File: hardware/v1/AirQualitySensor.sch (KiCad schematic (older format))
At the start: 1 part

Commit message: Start schematic
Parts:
- added DS1: EA_DOGM132W-5, AirQualitySensor:EA_DOGM132W-5, symbol AirQualitySensor:EA_DOGM132W-5
- added U1: 004-0-0053, AirQualitySensor:Senseair_S8_Up, symbol AirQualitySensor:004-0-0053
- added U2: DHT22, AirQualitySensor:DHT22, symbol AirQualitySensor:DHT22
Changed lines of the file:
@@
 NoConn ~ 5000 2150
 NoConn ~ 5000 2050
+$Comp
+L AirQualitySensor:EA_DOGM132W-5 DS1
+U 1 1 615E0422
+P 7350 2150
+F 0 "DS1" H 7950 2415 50  0000 C CNN
+F 1 "EA_DOGM132W-5" H 7950 2324 50  0000 C CNN
+F 2 "AirQualitySensor:EA_DOGM132W-5" H 8400 2250 50  0001 L CNN
+F 3 "" H 8400 2150 50  0001 L CNN
+F 4 "LCD Graphic Display Modules & Accessories DOGM Grapic 132x32 White Background" H 8400 2050 50  0001 L CNN "Description"
+F 5 "2" H 8400 1950 50  0001 L CNN "Height"
+F 6 "790-EADOGM132W5" H 8400 1850 50  0001 L CNN "Mouser Part Number"
+F 7 "https://www.mouser.co.uk/ProductDetail/ELECTRONIC-ASSEMBLY/EA-DOGM132W-5?qs=s9z6UkyjM7o689ToJkW0yA%3D%3D" H 8400 1750 50  0001 L CNN "Mouser Price/Stock"
+F 8 "ELECTRONIC ASSEMBLY" H 8400 1650 50  0001 L CNN "Manufacturer_Name"
+F 9 "EA DOGM132W-5" H 8400 1550 50  0001 L CNN "Manufacturer_Part_Number"
+	1    7350 2150
+	1    0    0    -1
+$EndComp
+$Comp
+L AirQualitySensor:004-0-0053 U1
+U 1 1 615E61D2
+P 3950 5000
+F 0 "U1" H 3950 5581 50  0000 C CNN
+F 1 "004-0-0053" H 3950 5490 50  0000 C CNN
+F 2 "AirQualitySensor:Senseair_S8_Up" H 3950 5000 50  0001 C CNN
+F 3 "https://rmtplusstoragesenseair.blob.core.windows.net/docs/publicerat/PSP126.pdf" H 3950 5000 50  0001 C CNN
+	1    3950 5000
+	1    0    0    -1
+$EndComp
+$Comp
+L AirQualitySensor:DHT22 U2
+U 1 1 615E6A6B
+P 5750 4550
+F 0 "U2" H 6278 4446 50  0000 L CNN
+F 1 "DHT22" H 6278 4355 50  0000 L CNN
+F 2 "AirQualitySensor:DHT22" H 6500 4050 50  0001 C CNN
+F 3 "https://www.sparkfun.com/datasheets/Sensors/Temperature/DHT22.pdf" H 6500 4050 50  0001 C CNN
+	1    5750 4550
+	1    0    0    -1
+$EndComp
 $EndSCHEMATC

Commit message: More Layout work
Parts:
- added C1, C2: 1u, Capacitor_SMD:C_0603_1608Metric, symbol Device:C_Small
- added C10, C11, C12, C13, C6, C7, C8, C9: 1u, Capacitor_SMD:C_0402_1005Metric, symbol Device:C_Small
- added C3, C4: 4u7, Capacitor_SMD:C_0603_1608Metric, symbol Device:C_Small
- added C5: 100u, Capacitor_SMD:C_0402_1005Metric, symbol Device:C_Small
- added FB1, FB2: 100R, Inductor_SMD:L_0603_1608Metric, symbol Device:Ferrite_Bead_Small
- added J1: USB_C_Receptacle_USB2.0, Connector_USB:USB_C_Receptacle_HRO_TYPE-C-31-M-12, symbol Connector:USB_C_Receptacle_USB2.0
- added R1, R2: 5.1k, Resistor_SMD:R_0402_1005Metric, symbol Device:R_Small
- added R3, R4, R5: 10k, Resistor_SMD:R_0402_1005Metric, symbol Device:R_Small
- added U3: XC6206P332MR, Package_TO_SOT_SMD:SOT-23, symbol Regulator_Linear:XC6206PxxxMR
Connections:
- net +3V3: now also DS1.34 (VDD2), DS1.35 (VDD), C2.1, C4.1, C5.1, R3.1, R4.1, R5.1, U3.2 (VO)
- net +5V: now also U1.1 (G+), U2.1 (VDD), C3.1, FB1.1; no longer A1.22 (VBUS)
- net GND: now also DS1.26 (VSS_1), DS1.33 (VSS_2), U1.2 (G0), U2.4 (GND), C1.1, C10.1, C11.1, C12.2, C13.1, C2.2, C3.2, C4.2, C5.2, C6.1, C8.1, J1.A1 (GND), J1.A12 (GND), J1.B1 (GND), J1.B12 (GND), R1.2, R2.1, U3.1 (GND)
- net USB_D-: now reaches A1.23 (D-)
- net USB_D-: now also J1.A7 (D-), J1.B7 (D-)
- net USB_D+: now reaches A1.24 (D+)
- net USB_D+: now also J1.A6 (D+), J1.B6 (D+)
- net at DS1.21 (V0): now also C13.2
- net at DS1.22 (V1): now also C11.2
- net at DS1.23 (V2): now also C10.2
- net at DS1.24 (V3): now also C8.2
- net at DS1.25 (V4): now also C6.2
- net at DS1.27 (CAP2N): now also C7.1
- net at DS1.28 (CAP2P): now also C7.2
- net at DS1.29 (CAP1P): now also C9.1
- net at DS1.30 (CAP1N): now also C9.2
- net at DS1.31 (CAP3P): now also DS1.32 (VOUT), C12.1
- net DISP_SI: now reaches DS1.36 (SI)
- net DISP_SCL: now reaches DS1.37 (SCL)
- net DISP_A0: now reaches DS1.38 (A0)
- net DISP_RST: now reaches DS1.39 (RST)
- net DISP_CS: now reaches DS1.40 (CS1B)
- net S8_RXD: now reaches U1.7 (UART_TXD)
- net S8_RXD: now also R3.2
- net S8_TXD: now reaches U1.8 (UART_RXD)
- net S8_TXD: now also R4.2
- net DHT22: now reaches U2.2 (DATA)
- net DHT22: now also R5.2
- new net: J1.A5 (CC1), R1.1
- new net: J1.B5 (CC2), R2.2
- new net: C1.2, FB2.1, U3.3 (VI)
- new net VBUS: A1.22 (VBUS), FB1.2, FB2.2, J1.A4 (VBUS), J1.A9 (VBUS), J1.B4 (VBUS), J1.B9 (VBUS)
- no-connect marks 28 -> 40
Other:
- moved on the sheet: A1, DS1, U1, U2

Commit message: Continue schematic
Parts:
- added C14: 100u, Capacitor_SMD:C_0402_1005Metric, symbol Device:C_Small
- added J2: SWD, AirQualitySensor:TC2030-IDC-FP, symbol AirQualitySensor:TC2030
- added J3: UART, Connector_PinHeader_2.54mm:PinHeader_1x06_P2.54mm_Vertical, symbol AirQualitySensor:UART_ftdi
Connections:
- net +3V3: now also C14.2, J2.1 (VCC)
- net GND: now also C14.1, J2.5 (GND), J3.1 (GND)
- net VBUS: now also J3.3 (VCC)
- net RESET: now reaches A1.21 (P0.18/Reset)
- net RESET: now also J2.3 (nRESET)
- net SWD_SWO: now reaches A1.27 (SWO/P1.00)
- net SWD_SWO: now also J2.6 (SWO)
- net SWD_SWCLK: now reaches A1.31 (SWDCLK)
- net SWD_SWCLK: now also J2.4 (SWCLK)
- net SWD_SWDIO: now reaches A1.32 (SWDIO)
- net SWD_SWDIO: now also J2.2 (SWDIO)
- new net UART_RXD: J3.4 (TXD)
- new net UART_TXD: J3.5 (RXD)
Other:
- note added: "Display"
- note added: "Power & USB"
- note added: "Programming Connectors"
- note added: "Sensors"
- moved on the sheet: A1, C1, C10, C11, C12, C13, C2, C3, C4, C5, C6, C7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

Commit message: More layouting
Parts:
- added D1: Red, LED_THT:LED_D3.0mm, symbol Device:LED_Small
- added D2: Yellow, LED_THT:LED_D3.0mm, symbol Device:LED_Small
- added D3: Green, LED_THT:LED_D3.0mm, symbol Device:LED_Small
- added H1, H2, H3: MountingHole, MountingHole:MountingHole_2.5mm_Pad, symbol Mechanical:MountingHole_Pad
- added R6, R7: 10k, Resistor_SMD:R_0402_1005Metric, symbol Device:R_Small
- added R8: 100k, Resistor_SMD:R_0402_1005Metric, symbol Device:R_Small
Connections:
- net +3V3: now also C14.1, C5.2; no longer C14.2, C5.1
- net GND: now also C10.2, C11.2, C12.1, C13.2, C14.2, C5.1, C6.2, C8.2, R2.2, D1.1 (K), D2.1 (K), D3.1 (K); no longer C10.1, C11.1, C12.2, C13.1, C14.1, C5.2, C6.1, C8.1, R2.1
- net at DS1.21 (V0): now also C13.1; no longer C13.2
- net at DS1.22 (V1): now also C11.1; no longer C11.2
- net at DS1.23 (V2): now also C10.1; no longer C10.2
- net at DS1.24 (V3): now also C8.1; no longer C8.2
- net at DS1.25 (V4): now also C6.1; no longer C6.2
- net at DS1.27 (CAP2N): now also C7.2; no longer C7.1
- net at DS1.28 (CAP2P): now also C7.1; no longer C7.2
- net at DS1.29 (CAP1P): now also C9.2; no longer C9.1
- net at DS1.30 (CAP1N): now also C9.1; no longer C9.2
- net at DS1.31 (CAP3P), DS1.32 (VOUT): now also C12.2; no longer C12.1
- net at J1.B5 (CC2): now also R2.1; no longer R2.2
- new net: D1.2 (A), R6.1
- new net: D2.2 (A), R7.1
- new net: D3.2 (A), R8.1
- new net LED_GREEN: R8.2
- new net LED_RED: R6.2
- new net LED_YELLOW: R7.2
- no-connect marks 40 -> 43
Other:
- note added: "LEDs"
- moved on the sheet: C14
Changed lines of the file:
@@
 U 1 1 616037F6
 P 2100 1350
-F 0 "R2" H 2150 1450 50  0000 L CNN
-F 1 "5.1k" V 2200 1200 50  0000 L CNN
+F 0 "R2" H 2150 1250 50  0000 L CNN
+F 1 "5.1k" V 2200 1500 50  0000 R CNN
 F 2 "Resistor_SMD:R_0402_1005Metric" H 2100 1350 50  0001 C CNN
 F 3 "~" H 2100 1350 50  0001 C CNN
 	1    2100 1350
-	0    1    1    0
+	0    -1   1    0
 $EndComp
 $Comp
@@
 F 3 "~" H 8950 2800 50  0001 C CNN
 	1    8950 2800
-	-1   0    0    1
+	-1   0    0    -1
 $EndComp
 $Comp
@@
 F 3 "~" H 8700 2700 50  0001 C CNN
 	1    8700 2700
-	-1   0    0    1
+	-1   0    0    -1
 $EndComp
 $Comp
@@
 F 3 "~" H 9200 2900 50  0001 C CNN
 	1    9200 2900
-	-1   0    0    1
+	-1   0    0    -1
 $EndComp
 $Comp
@@
 F 3 "~" H 9450 3000 50  0001 C CNN
 	1    9450 3000
-	-1   0    0    1
+	-1   0    0    -1
 $EndComp
 $Comp
@@
 F 3 "~" H 9700 3100 50  0001 C CNN
 	1    9700 3100
-	-1   0    0    1
+	-1   0    0    -1
 $EndComp
 Wire Wire Line
@@
 F 3 "~" H 9500 1850 50  0001 C CNN
 	1    9500 1850
-	-1   0    0    1
+	-1   0    0    -1
 $EndComp
 Wire Wire Line
@@
 F 3 "~" H 9100 2050 50  0001 C CNN
 	1    9100 2050
-	0    -1   1    0
+	0    1    1    0
 $EndComp
 $Comp
@@
 F 3 "~" H 8850 2250 50  0001 C CNN
 	1    8850 2250
-	0    -1   -1   0
+	0    1    -1   0
 $EndComp
 Wire Wire Line
@@
 Wire Wire Line
 	9000 2150 9000 2050
-Wire Wire Line
-	9000 2150 9750 2150
 Wire Wire Line
 	9750 2250 8950 2250
@@
 F 3 "~" H 5350 5450 50  0001 C CNN
 	1    5350 5450
-	1    0    0    -1
+	1    0    0    1
 $EndComp
 $Comp
@@
 Wire Wire Line
 	5350 5200 5350 5350
-Connection ~ 5350 5350
 Wire Wire Line
 	5250 5350 5350 5350
-Wire Wire Line
-	8750 2350 9750 2350
-Wire Wire Line
-	9350 1750 9500 1750
-Connection ~ 9500 1750
-Wire Wire Line
-	9500 1750 9750 1750
 $Comp
 L AirQualitySensor:TC2030 J2
@@
 L Device:C_Small C14
 U 1 1 617462A1
-P 8950 1150
-F 0 "C14" H 9042 1196 50  0000 L CNN
-F 1 "100u" H 9042 1105 50  0000 L CNN
-F 2 "Capacitor_SMD:C_0402_1005Metric" H 8950 1150 50  0001 C CNN
-F 3 "~" H 8950 1150 50  0001 C CNN
-	1    8950 1150
-	-1   0    0    1
+P 8850 1150
+F 0 "C14" H 8942 1196 50  0000 L CNN
+F 1 "100u" H 8942 1105 50  0000 L CNN
+F 2 "Capacitor_SMD:C_0402_1005Metric" H 8850 1150 50  0001 C CNN
+F 3 "~" H 8850 1150 50  0001 C CNN
+	1    8850 1150
+	1    0    0    -1
 $EndComp
 $Comp
 L power:+3V3 #PWR0129
 U 1 1 617473D8
-P 8950 1050
-F 0 "#PWR0129" H 8950 900 50  0001 C CNN
-F 1 "+3V3" H 8800 1150 50  0000 C CNN
-F 2 "" H 8950 1050 50  0001 C CNN
-F 3 "" H 8950 1050 50  0001 C CNN
-	1    8950 1050
+P 8850 1050
+F 0 "#PWR0129" H 8850 900 50  0001 C CNN
+F 1 "+3V3" H 8700 1150 50  0000 C CNN
+F 2 "" H 8850 1050 50  0001 C CNN
+F 3 "" H 8850 1050 50  0001 C CNN
+	1    8850 1050
 	1    0    0    -1
 $EndComp
@@
 L power:GND #PWR0130
 U 1 1 6174788F
-P 8950 1250
-F 0 "#PWR0130" H 8950 1000 50  0001 C CNN
-F 1 "GND" H 9000 1100 50  0000 R CNN
-F 2 "" H 8950 1250 50  0001 C CNN
-F 3 "" H 8950 1250 50  0001 C CNN
-	1    8950 1250
-	1    0    0    -1
-$EndComp
+P 8850 1250
+F 0 "#PWR0130" H 8850 1000 50  0001 C CNN
+F 1 "GND" H 8900 1100 50  0000 R CNN
+F 2 "" H 8850 1250 50  0001 C CNN
+F 3 "" H 8850 1250 50  0001 C CNN
+	1    8850 1250
+	1    0    0    -1
+$EndComp
+$Comp
+L Device:LED_Small D1
+U 1 1 61768156
+P 1050 5600
+F 0 "D1" V 1096 5530 50  0000 R CNN
+F 1 "Red" V 1005 5530 50  0000 R CNN
+F 2 "LED_THT:LED_D3.0mm" V 1050 5600 50  0001 C CNN
+F 3 "~" V 1050 5600 50  0001 C CNN
+	1    1050 5600
+	0    -1   -1   0
+$EndComp
+$Comp
+L Device:LED_Small D2
+U 1 1 61768FD8
+P 1500 5600
+F 0 "D2" V 1546 5530 50  0000 R CNN
+F 1 "Yellow" V 1455 5530 50  0000 R CNN
+F 2 "LED_THT:LED_D3.0mm" V 1500 5600 50  0001 C CNN
+F 3 "~" V 1500 5600 50  0001 C CNN
+	1    1500 5600
+	0    -1   -1   0
+$EndComp
+$Comp
+L Device:LED_Small D3
+U 1 1 617694C1
+P 1950 5600
+F 0 "D3" V 1996 5530 50  0000 R CNN
+F 1 "Green" V 1905 5530 50  0000 R CNN
+F 2 "LED_THT:LED_D3.0mm" V 1950 5600 50  0001 C CNN
+F 3 "~" V 1950 5600 50  0001 C CNN
+	1    1950 5600
+	0    -1   -1   0
+$EndComp
+$Comp
+L Device:R_Small R8
+U 1 1 61776347
+P 1950 5400
+F 0 "R8" H 1891 5354 50  0000 R CNN
+F 1 "100k" H 1891 5445 50  0000 R CNN
+F 2 "Resistor_SMD:R_0402_1005Metric" H 1950 5400 50  0001 C CNN
+F 3 "~" H 1950 5400 50  0001 C CNN
+	1    1950 5400
+	-1   0    0    1
+$EndComp
+$Comp
+L Device:R_Small R7
+U 1 1 61776CEE
+P 1500 5400
+F 0 "R7" H 1441 5354 50  0000 R CNN
+F 1 "10k" H 1441 5445 50  0000 R CNN
+F 2 "Resistor_SMD:R_0402_1005Metric" H 1500 5400 50  0001 C CNN
+F 3 "~" H 1500 5400 50  0001 C CNN
+	1    1500 5400
+	-1   0    0    1
+$EndComp
+$Comp
+L Device:R_Small R6
+U 1 1 61776FAB
+P 1050 5400
+F 0 "R6" H 991 5354 50  0000 R CNN
+F 1 "10k" H 991 5445 50  0000 R CNN
+F 2 "Resistor_SMD:R_0402_1005Metric" H 1050 5400 50  0001 C CNN
+F 3 "~" H 1050 5400 50  0001 C CNN
+	1    1050 5400
+	-1   0    0    1
+$EndComp
+$Comp
+L power:GND #PWR0131
+U 1 1 617BCF08
+P 1050 5700
+F 0 "#PWR0131" H 1050 5450 50  0001 C CNN
+F 1 "GND" H 1000 5650 50  0000 R CNN
+F 2 "" H 1050 5700 50  0001 C CNN
+F 3 "" H 1050 5700 50  0001 C CNN
+	1    1050 5700
+	1    0    0    -1
+$EndComp
+$Comp
+L power:GND #PWR0132
+U 1 1 617BD3BE
+P 1500 5700
+F 0 "#PWR0132" H 1500 5450 50  0001 C CNN
+F 1 "GND" H 1450 5650 50  0000 R CNN
+F 2 "" H 1500 5700 50  0001 C CNN
+F 3 "" H 1500 5700 50  0001 C CNN
+	1    1500 5700
+	1    0    0    -1
+$EndComp
+$Comp
+L power:GND #PWR0133
+U 1 1 617BD55D
+P 1950 5700
+F 0 "#PWR0133" H 1950 5450 50  0001 C CNN
+F 1 "GND" H 1900 5650 50  0000 R CNN
+F 2 "" H 1950 5700 50  0001 C CNN
+F 3 "" H 1950 5700 50  0001 C CNN
+	1    1950 5700
+	1    0    0    -1
+$EndComp
+Text GLabel 1050 5250 1    50   Input ~ 0
+LED_RED
+Text GLabel 1500 5250 1    50   Input ~ 0
+LED_YELLOW
+Text GLabel 1950 5250 1    50   Input ~ 0
+LED_GREEN
+Wire Wire Line
+	1950 5250 1950 5300
+Wire Wire Line
+	1500 5250 1500 5300
+Wire Wire Line
+	1050 5250 1050 5300
+Wire Notes Line
+	750  4650 2300 4650
+Wire Notes Line
+	2300 4650 2300 5900
+Wire Notes Line
+	2300 5900 750  5900
+Wire Notes Line
+	750  5900 750  4650
+Text Notes 750  4650 0    50   ~ 0
+LEDs
+$Comp
+L Mechanical:MountingHole_Pad H1
+U 1 1 6181BCA6
+P 950 3800
+F 0 "H1" V 904 3950 50  0000 L CNN
+F 1 "MountingHole" V 995 3950 50  0000 L CNN
+F 2 "MountingHole:MountingHole_2.5mm_Pad" H 950 3800 50  0001 C CNN
+F 3 "~" H 950 3800 50  0001 C CNN
+	1    950  3800
+	0    1    1    0
+$EndComp
+$Comp
+L Mechanical:MountingHole_Pad H2
+U 1 1 6181ED3E
+P 950 4000
+F 0 "H2" V 904 4150 50  0000 L CNN
+F 1 "MountingHole" V 995 4150 50  0000 L CNN
+F 2 "MountingHole:MountingHole_2.5mm_Pad" H 950 4000 50  0001 C CNN
+F 3 "~" H 950 4000 50  0001 C CNN
+	1    950  4000
+	0    1    1    0
+$EndComp
+$Comp
+L Mechanical:MountingHole_Pad H3
+U 1 1 6181F050
+P 950 4200
+F 0 "H3" V 904 4350 50  0000 L CNN
+F 1 "MountingHole" V 995 4350 50  0000 L CNN
+F 2 "MountingHole:MountingHole_2.5mm_Pad" H 950 4200 50  0001 C CNN
+F 3 "~" H 950 4200 50  0001 C CNN
+	1    950  4200
+	0    1    1    0
+$EndComp
+NoConn ~ 850  3800
+NoConn ~ 850  4000
+NoConn ~ 850  4200
+Wire Wire Line
+	9000 2150 9750 2150
+Wire Wire Line
+	8750 2350 9750 2350
+Wire Wire Line
+	9350 1750 9500 1750
+Connection ~ 9500 1750
+Wire Wire Line
+	9500 1750 9750 1750
+Connection ~ 5350 5350
 $EndSCHEMATC

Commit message: More layouting
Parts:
- added R10, R9: 10k, Resistor_SMD:R_0402_1005Metric, symbol Device:R_Small
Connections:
- wire segments 106 -> 127
- no-connect marks 43 -> 30
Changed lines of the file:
@@
 L power:GND #PWR0102
 U 1 1 615D7DF8
-P 4750 3700
-F 0 "#PWR0102" H 4750 3450 50  0001 C CNN
-F 1 "GND" V 4650 3700 50  0000 R CNN
-F 2 "" H 4750 3700 50  0001 C CNN
-F 3 "" H 4750 3700 50  0001 C CNN
-	1    4750 3700
+P 4100 3700
+F 0 "#PWR0102" H 4100 3450 50  0001 C CNN
+F 1 "GND" V 4000 3700 50  0000 R CNN
+F 2 "" H 4100 3700 50  0001 C CNN
+F 3 "" H 4100 3700 50  0001 C CNN
+	1    4100 3700
 	1    0    0    -1
 $EndComp
@@
 	1    0    0    -1
 $EndComp
-NoConn ~ 4850 3800
-NoConn ~ 4850 3900
 NoConn ~ 4850 4000
 NoConn ~ 4850 4100
 NoConn ~ 4850 4200
 NoConn ~ 4850 4300
-NoConn ~ 4850 4400
-NoConn ~ 4850 4500
-NoConn ~ 4850 4600
-NoConn ~ 4850 4700
-NoConn ~ 4850 4800
 NoConn ~ 4850 4900
 NoConn ~ 5450 5200
-NoConn ~ 5550 5200
-NoConn ~ 5650 5200
-NoConn ~ 5750 5200
-NoConn ~ 5850 5200
-NoConn ~ 5950 5200
 $Comp
 L power:+3V3 #PWR0105
@@
 NoConn ~ 6850 4400
 NoConn ~ 6850 4100
-NoConn ~ 6850 4000
 NoConn ~ 6850 3900
 NoConn ~ 6850 3800
@@
 F 3 "~" H 5350 5450 50  0001 C CNN
 	1    5350 5450
-	1    0    0    1
+	-1   0    0    1
 $EndComp
 $Comp
@@
 	6950 3700 6850 3700
 Wire Wire Line
-	4750 3700 4850 3700
+	4100 3700 4850 3700
 Wire Wire Line
 	6850 4900 6950 4900
@@
 Wire Wire Line
 	10100 5700 10100 5450
-Text GLabel 10000 5800 0    50   Input ~ 0
+Text GLabel 9650 5800 0    50   Input ~ 0
 UART_RXD
 Wire Wire Line
-	10000 5800 10200 5800
-Text GLabel 10000 5900 0    50   Input ~ 0
+	9650 5800 9750 5800
+Text GLabel 9650 5900 0    50   Input ~ 0
 UART_TXD
 Wire Wire Line
-	10000 5900 10200 5900
+	9650 5900 9850 5900
 NoConn ~ 10200 5600
 NoConn ~ 10200 6000
@@
 	9500 1750 9750 1750
 Connection ~ 5350 5350
+Text GLabel 7050 4000 2    50   Input ~ 0
+DHT22
+Wire Wire Line
+	7050 4000 6850 4000
+Text GLabel 5950 5450 3    50   Input ~ 0
+DISP_SI
+Text GLabel 5850 5450 3    50   Input ~ 0
+DISP_SCL
+Text GLabel 5750 5450 3    50   Input ~ 0
+DISP_A0
+Text GLabel 5650 5450 3    50   Input ~ 0
+DISP_RST
+Wire Wire Line
+	5550 5450 5550 5200
+Wire Wire Line
+	5650 5450 5650 5200
+Wire Wire Line
+	5750 5450 5750 5200
+Wire Wire Line
+	5850 5450 5850 5200
+Wire Wire Line
+	5950 5450 5950 5200
+Text GLabel 5550 5450 3    50   Input ~ 0
+DISP_CS
+$Comp
+L Device:R_Small R9
+U 1 1 619F8BB8
+P 9750 5550
+F 0 "R9" H 9700 5500 50  0000 R CNN
+F 1 "10k" H 9700 5600 50  0000 R CNN
+F 2 "Resistor_SMD:R_0402_1005Metric" H 9750 5550 50  0001 C CNN
+F 3 "~" H 9750 5550 50  0001 C CNN
+	1    9750 5550
+	1    0    0    -1
+$EndComp
+$Comp
+L Device:R_Small R10
+U 1 1 619F8BC2
+P 9850 5550
+F 0 "R10" H 9800 5500 50  0000 R CNN
+F 1 "10k" H 9800 5600 50  0000 R CNN
+F 2 "Resistor_SMD:R_0402_1005Metric" H 9850 5550 50  0001 C CNN
+F 3 "~" H 9850 5550 50  0001 C CNN
+	1    9850 5550
+	-1   0    0    1
+$EndComp
+Wire Wire Line
+	9750 5800 9750 5650
+Wire Wire Line
+	9850 5900 9850 5650
+Wire Wire Line
+	9750 5450 9750 5400
+Wire Wire Line
+	9750 5400 9800 5400
+Wire Wire Line
+	9850 5400 9850 5450
+$Comp
+L power:+3V3 #PWR0134
+U 1 1 619F8BD1
+P 9800 5400
+F 0 "#PWR0134" H 9800 5250 50  0001 C CNN
+F 1 "+3V3" H 9815 5573 50  0000 C CNN
+F 2 "" H 9800 5400 50  0001 C CNN
+F 3 "" H 9800 5400 50  0001 C CNN
+	1    9800 5400
+	1    0    0    -1
+$EndComp
+Connection ~ 9800 5400
+Wire Wire Line
+	9800 5400 9850 5400
+Connection ~ 9750 5800
+Wire Wire Line
+	9750 5800 10200 5800
+Connection ~ 9850 5900
+Wire Wire Line
+	9850 5900 10200 5900
+Text GLabel 4700 3900 0    50   Input ~ 0
+UART_RXD
+Wire Wire Line
+	4700 3800 4850 3800
+Text GLabel 4700 3800 0    50   Input ~ 0
+UART_TXD
+Wire Wire Line
+	4700 3900 4850 3900
+Text GLabel 4700 4400 0    50   Input ~ 0
+S8_RXD
+Text GLabel 4700 4500 0    50   Input ~ 0
+S8_TXD
+Wire Wire Line
+	4700 4500 4850 4500
+Wire Wire Line
+	4850 4400 4700 4400
+Text GLabel 4700 4800 0    50   Input ~ 0
+LED_RED
+Text GLabel 4700 4700 0    50   Input ~ 0
+LED_YELLOW
+Text GLabel 4700 4600 0    50   Input ~ 0
+LED_GREEN
+Wire Wire Line
+	4850 4600 4700 4600
+Wire Wire Line
+	4700 4700 4850 4700
+Wire Wire Line
+	4850 4800 4700 4800
 $EndSCHEMATC

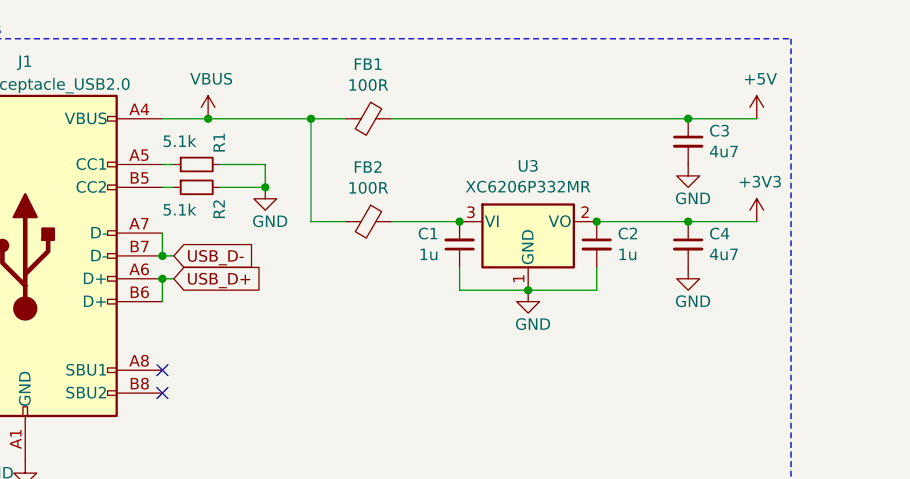
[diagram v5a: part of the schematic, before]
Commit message: Finish first layout
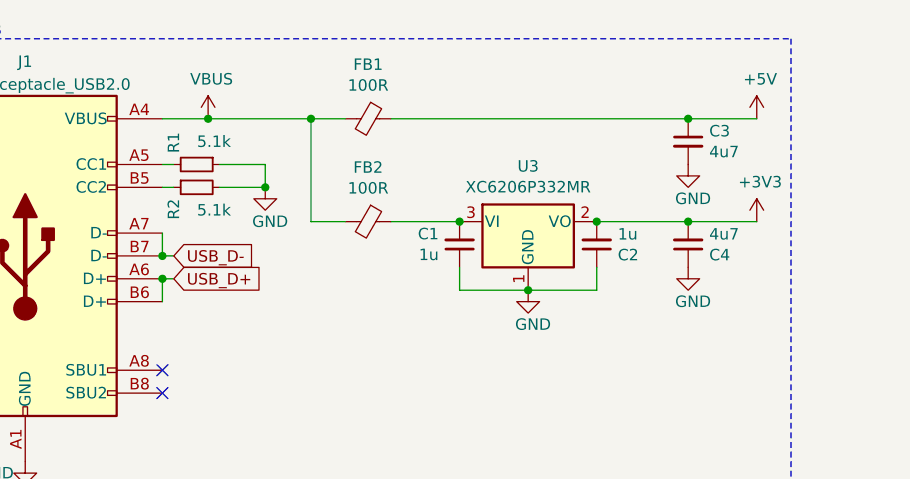
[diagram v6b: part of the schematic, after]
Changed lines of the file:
@@
-$EndComp
-$Comp
-L AirQualitySensor:DHT22 U2
-U 1 1 615E6A6B
-P 3800 6750
-F 0 "U2" H 4328 6646 50  0000 L CNN
-F 1 "DHT22" H 4328 6555 50  0000 L CNN
-F 2 "AirQualitySensor:DHT22" H 4550 6250 50  0001 C CNN
-F 3 "https://www.sparkfun.com/datasheets/Sensors/Temperature/DHT22.pdf" H 4550 6250 50  0001 C CNN
-	1    3800 6750
-	1    0    0    -1
 $EndComp
 $Comp
@@
 U 1 1 616037F6
 P 2100 1350
-F 0 "R2" H 2150 1250 50  0000 L CNN
-F 1 "5.1k" V 2200 1500 50  0000 R CNN
+F 0 "R2" H 2150 1450 50  0000 L CNN
+F 1 "5.1k" V 2200 1200 50  0000 L CNN
 F 2 "Resistor_SMD:R_0402_1005Metric" H 2100 1350 50  0001 C CNN
 F 3 "~" H 2100 1350 50  0001 C CNN
@@
 F 3 "~" H 2100 1250 50  0001 C CNN
 	1    2100 1250
-	0    -1   1    0
+	0    1    1    0
 $EndComp
 Wire Wire Line
@@
 F 3 "~" H 3850 1600 50  0001 C CNN
 	1    3850 1600
-	1    0    0    -1
+	1    0    0    1
 $EndComp
 $Comp
@@
 Wire Wire Line
 	2950 1050 4250 1050
-Wire Wire Line
-	3850 1500 4250 1500
-Connection ~ 3850 1500
 $Comp
 L Device:C_Small C3
@@
 F 3 "~" H 4250 1600 50  0001 C CNN
 	1    4250 1600
-	1    0    0    -1
+	1    0    0    1
 $EndComp
 $Comp
@@
 	1    0    0    -1
 $EndComp
-Wire Wire Line
-	4250 1500 4550 1500
-Connection ~ 4250 1500
 Wire Wire Line
 	4250 1050 4550 1050
@@
 Wire Wire Line
 	4850 4800 4700 4800
+Connection ~ 3850 1500
+Wire Wire Line
+	3850 1500 4250 1500
+Connection ~ 4250 1500
+Wire Wire Line
+	4250 1500 4550 1500
+$Comp
+L AirQualitySensor:DHT22 U2
+U 1 1 615E6A6B
+P 3800 6750
+F 0 "U2" H 4328 6646 50  0000 L CNN
+F 1 "DHT22" H 4328 6555 50  0000 L CNN
+F 2 "AirQualitySensor:DHT22" H 4550 6250 50  0001 C CNN
+F 3 "https://www.sparkfun.com/datasheets/Sensors/Temperature/DHT22.pdf" H 4550 6250 50  0001 C CNN
+	1    3800 6750
+	1    0    0    -1
+$EndComp
 $EndSCHEMATC
